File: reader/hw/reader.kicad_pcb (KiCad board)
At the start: 2 copper layers, 50 x 50 mm, 41 parts, among them P101 Wago_233-502, P102 Wago_233-502, P103 CONN_02X05, P104 JST, P105 CONN_01X08, Q101 MMBT2222A, Q102 MMBT2222A, U101 LP2992AIM5-3.3CT-ND, U102 SN75176BDR, U103 MKE04P24M48SF0, X101 CRYSTAL

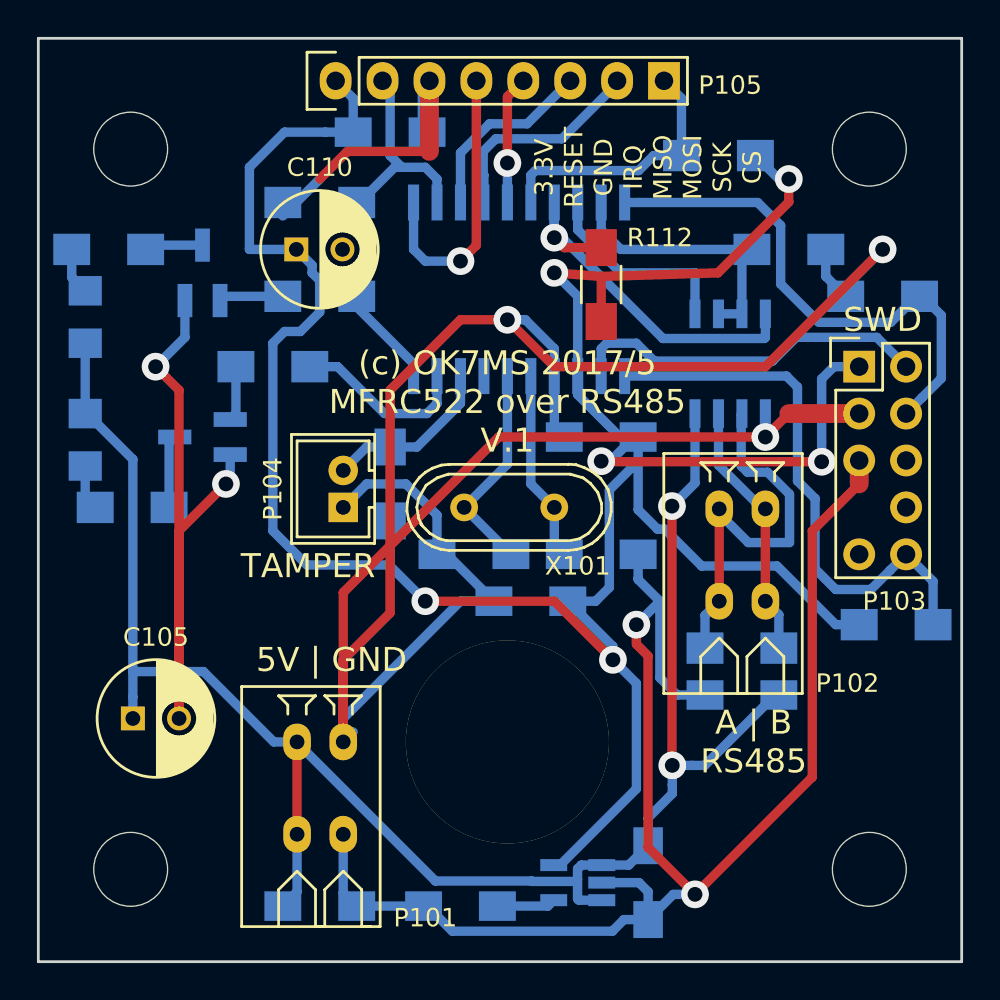
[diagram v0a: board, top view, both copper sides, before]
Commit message: Fix MISO/TAMPER issue, fix watchdog, fix corruption when SPI cmd + 1 byte data
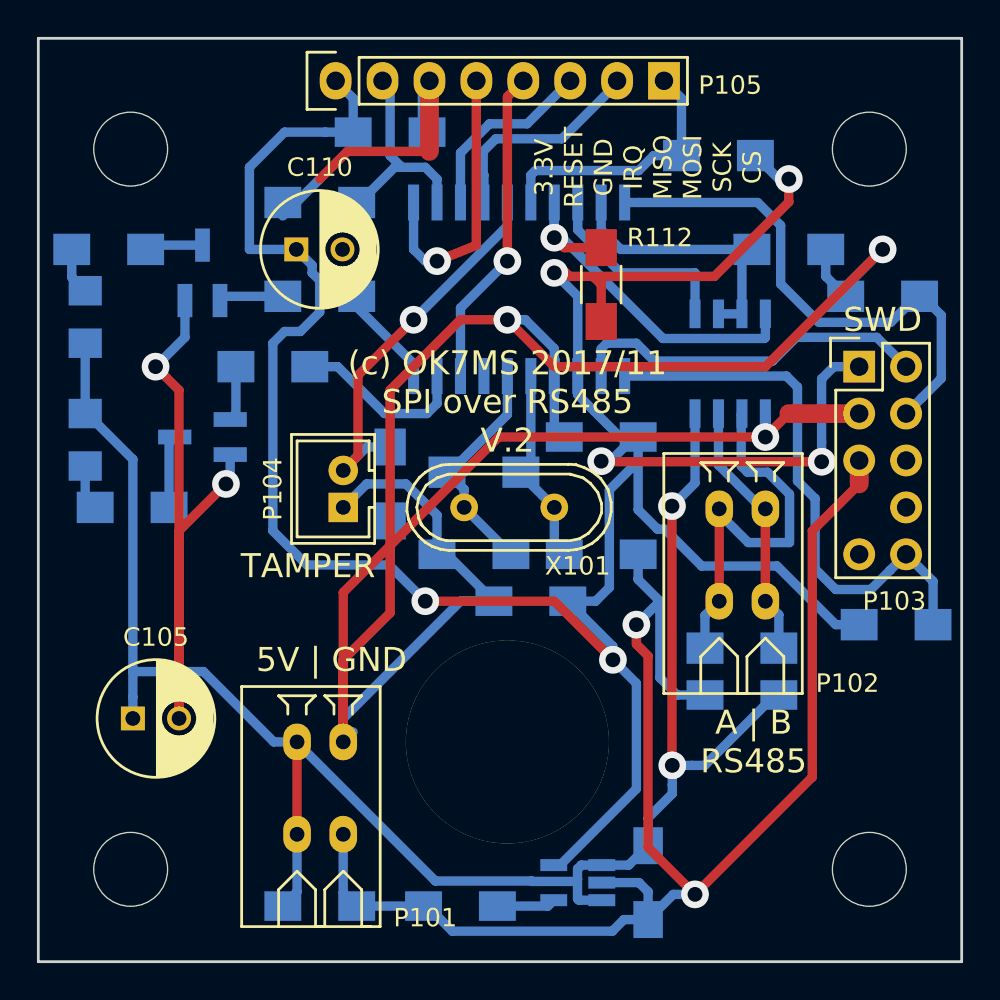
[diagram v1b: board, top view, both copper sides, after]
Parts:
- added R113: 10M, smd-handsolder:R_1206_HandSoldering, B.Cu at (74.1, 73.5)
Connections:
- U103 pad 15: /MISO -> /TAMPER
- U103 pad 8: /TAMPER -> /MISO
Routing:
- net /TAMPER: track 9.34 -> 21.3 mm, vias 0 -> 1
- net /MISO: track 6.95 -> 17.4 mm
- net Net-(C108-Pad1): track 11.7 -> 12.5 mm
- net +3V3: track 157.0 -> 157.8 mm
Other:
- board text added: "(c) OK7MS 2017/11 SPI over RS485 V.2"
- board text removed: "(c) OK7MS 2017/5 MFRC522 over RS485 V.1"
